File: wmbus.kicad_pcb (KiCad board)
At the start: 2 copper layers, 27 parts, among them IC1 IM871A, J1 480-37-1000, J2 Conn_Coaxial, J3 Conn_01x04_Male, U1 USBLC6-2SC6, U2 XC6206P332MR, U3 CH340E

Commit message: Routing done
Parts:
- added G***: LOGO, LOGO, B.Cu at (105.1, 102.8)
- added kibuzzard-63642CB1: G***, kibuzzard-63642CB1, B.Cu at (108.1, 102.8)
- J2: footprint Connector_Coaxial:SMA_Amphenol_132289_EdgeMount -> wmbus:SMA-SMD_BWSMA-KE-P001
- moved J2 0.74 mm to (119.8, 102.8)
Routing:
- net +3.3V: track 0.00 -> 42.9 mm
- net GND: track 0.00 -> 27.3 mm, vias 0 -> 26
- net /UART_TX: track 0.00 -> 21.4 mm, vias 0 -> 2
- net Net-(D3-Pad2): track 0.00 -> 20.2 mm
- net /UART_RX: track 0.00 -> 18.1 mm, vias 0 -> 2
- net /DBG_CLK: track 0.00 -> 15.7 mm
- net /DBG_DATA: track 0.00 -> 12.9 mm
- net Net-(D2-Pad2): track 0.00 -> 11.9 mm
- net VBUS: track 0.00 -> 9.36 mm
- net Net-(JP2-Pad1): track 0.00 -> 8.10 mm
- net Net-(D1-Pad2): track 0.00 -> 7.48 mm
- net Net-(JP1-Pad1): track 0.00 -> 7.25 mm
- net Net-(C3-Pad1): track 0.00 -> 5.14 mm
- net /USB_CONN_D-: track 0.00 -> 3.61 mm
- net /USB_CONN_D+: track 0.00 -> 3.61 mm
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
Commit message: Ready for production rev1
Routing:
- net Net-(IC1-Pad16): track 0.00 -> 13.3 mm
- net GND: track 27.3 -> 30.3 mm, vias 26 -> 59
- added copper zone on In1.Cu, net GND
- added copper zone on In2.Cu, net GND
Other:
- board outline added: 56.6 x 20 mm
- copper layers 2 -> 4

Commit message: Added antenna 3D model, removed useless GND via, unified via size
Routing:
- net GND: track 30.3 -> 28.7 mm, vias 59 -> 58
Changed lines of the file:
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@@
     (pad "5" smd rect (at 0 2.55) (size 5 1.2) (layers "F.Cu" "F.Paste" "F.Mask")
       (net 16 "GND") (pinfunction "Ext") (pintype "passive"))
+    (model "${KIPRJMOD}/3D/antenna.wrl"
+      (offset (xyz 0 0 -4))
+      (scale (xyz 0.4 0.4 0.4))
+      (rotate (xyz 0 0 90))
+    )
   )
   (footprint "wmbus:MOLEX_480-37-1000" (layer "F.Cu")
@@
     (property "Sheetname" "")
     (attr through_hole)
-    (fp_text reference "J1" (at -2.825 -6.635 -90) (layer "F.SilkS")
+    (fp_text reference "J1" (at -2.825 -6.635 -90) (layer "F.SilkS") hide
       (effects (font (size 1 1) (thickness 0.15)))
     )
@@
   (segment (start 110.35 93.825) (end 110.35 94.925) (width 0.3) (layer "F.Cu") (net 16))
   (segment (start 84 109.575) (end 84 110.525) (width 0.3) (layer "F.Cu") (net 16))
-  (segment (start 82.575 95.65) (end 82.185 95.65) (width 0.3) (layer "F.Cu") (net 16))
   (segment (start 88.075 105.8) (end 87.1 105.8) (width 0.3) (layer "F.Cu") (net 16))
   (segment (start 77.025 109.575) (end 77.025 110.55) (width 0.3) (layer "F.Cu") (net 16))
@@
   (segment (start 86.185 110.175) (end 85.25 110.175) (width 0.3) (layer "F.Cu") (net 16))
   (segment (start 97.75 97.225) (end 96.475 97.225) (width 0.3) (layer "F.Cu") (net 16))
-  (segment (start 83.45 96.525) (end 82.575 95.65) (width 0.3) (layer "F.Cu") (net 16))
   (segment (start 86.185 108.575) (end 85.25 108.575) (width 0.3) (layer "F.Cu") (net 16))
   (segment (start 74.5625 102.5) (end 73.25 102.5) (width 0.3) (layer "F.Cu") (net 16))
   (segment (start 96.475 97.225) (end 96.45 97.2) (width 0.3) (layer "F.Cu") (net 16))
   (segment (start 85.25 110.175) (end 85.225 110.15) (width 0.3) (layer "F.Cu") (net 16))
-  (segment (start 75.5 109.575) (end 75.5 110.55) (width 0.3) (layer "F.Cu") (net 16))
   (segment (start 85.3 111.775) (end 86.185 111.775) (width 0.3) (layer "F.Cu") (net 16))
   (segment (start 119.75 99.125) (end 119.75 100.275) (width 0.3) (layer "F.Cu") (net 16))
@@
   (segment (start 95.27 104.72) (end 95.27 105.675) (width 0.3) (layer "F.Cu") (net 16))
   (segment (start 97.75 105.625) (end 96.525 105.625) (width 0.3) (layer "F.Cu") (net 16))
-  (segment (start 80.6875 110.7625) (end 80.675 110.775) (width 0.3) (layer "F.Cu") (net 16))
   (segment (start 114.55 94.925) (end 114.55 93.85) (width 0.3) (layer "F.Cu") (net 16))
   (segment (start 71.1 99) (end 71.1 97.875) (width 0.3) (layer "F.Cu") (net 16))
@@
   (segment (start 79.425 103.25) (end 80.675 103.25) (width 0.3) (layer "F.Cu") (net 16))
   (segment (start 85.275 111.75) (end 85.3 111.775) (width 0.3) (layer "F.Cu") (net 16))
+  (segment (start 75.5 109.575) (end 75.5 110.55) (width 0.3) (layer "F.Cu") (net 16))
   (segment (start 93.72 104.72) (end 93.72 105.675) (width 0.3) (layer "F.Cu") (net 16))
   (via (at 115.525 108.4) (size 0.7) (drill 0.3) (layers "F.Cu" "B.Cu") (net 16))
@@
   (via (at 119.725 96.125) (size 0.7) (drill 0.3) (layers "F.Cu" "B.Cu") (net 16))
   (via (at 96.45 97.2) (size 0.7) (drill 0.3) (layers "F.Cu" "B.Cu") (net 16))
-  (via (at 75.5 110.55) (size 0.8) (drill 0.4) (layers "F.Cu" "B.Cu") (net 16))
   (via (at 72.7 99) (size 0.7) (drill 0.3) (layers "F.Cu" "B.Cu") (net 16))
   (via (at 113.825 111.675) (size 0.7) (drill 0.3) (layers "F.Cu" "B.Cu") (net 16))
-  (via (at 80.675 110.775) (size 0.8) (drill 0.4) (layers "F.Cu" "B.Cu") (net 16))
-  (via (at 83.45 96.525) (size 0.7) (drill 0.3) (layers "F.Cu" "B.Cu") (net 16))
   (via (at 87.35 99.725) (size 0.7) (drill 0.3) (layers "F.Cu" "B.Cu") (net 16))
   (via (at 75.425 97.4) (size 0.7) (drill 0.3) (layers "F.Cu" "B.Cu") (net 16))
@@
   (via (at 115.725 103.575) (size 0.7) (drill 0.3) (layers "F.Cu" "B.Cu") (net 16))
   (via (at 78.8 111.475) (size 0.7) (drill 0.3) (layers "F.Cu" "B.Cu") (net 16))
+  (via (at 80.6875 110.7625) (size 0.7) (drill 0.3) (layers "F.Cu" "B.Cu") (net 16))
   (via (at 119.65 109.875) (size 0.7) (drill 0.3) (layers "F.Cu" "B.Cu") (net 16))
   (via (at 88.1 104.275) (size 0.7) (drill 0.3) (layers "F.Cu" "B.Cu") (net 16))
@@
   (via (at 95.25 104.7) (size 0.7) (drill 0.3) (layers "F.Cu" "B.Cu") (net 16))
   (via (at 85.275 111.75) (size 0.7) (drill 0.3) (layers "F.Cu" "B.Cu") (net 16))
-  (via (at 77.025 110.55) (size 0.8) (drill 0.4) (layers "F.Cu" "B.Cu") (net 16))
   (via (at 94.275 95.05) (size 0.7) (drill 0.3) (layers "F.Cu" "B.Cu") (net 16))
   (via (at 110.925 111.625) (size 0.7) (drill 0.3) (layers "F.Cu" "B.Cu") (net 16))
   (via (at 93.7 104.7) (size 0.7) (drill 0.3) (layers "F.Cu" "B.Cu") (net 16))
+  (via (at 75.5 110.55) (size 0.7) (drill 0.3) (layers "F.Cu" "B.Cu") (net 16))
   (via (at 119.75 99.125) (size 0.7) (drill 0.3) (layers "F.Cu" "B.Cu") (net 16))
   (via (at 78.875 106.1) (size 0.7) (drill 0.3) (layers "F.Cu" "B.Cu") (free) (net 16))
@@
   (via (at 85.225 110.15) (size 0.7) (drill 0.3) (layers "F.Cu" "B.Cu") (net 16))
   (via (at 117.525 97.425) (size 0.7) (drill 0.3) (layers "F.Cu" "B.Cu") (net 16))
+  (via (at 77.025 110.55) (size 0.7) (drill 0.3) (layers "F.Cu" "B.Cu") (net 16))
   (via (at 85.25 108.575) (size 0.7) (drill 0.3) (layers "F.Cu" "B.Cu") (net 16))
   (via (at 88.075 101.8) (size 0.7) (drill 0.3) (layers "F.Cu" "B.Cu") (net 16))

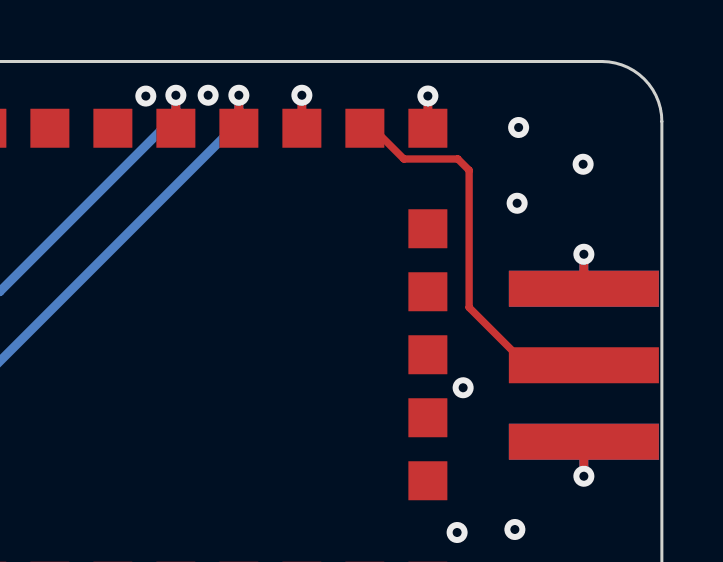
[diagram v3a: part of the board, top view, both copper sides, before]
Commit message: Rounded RF track
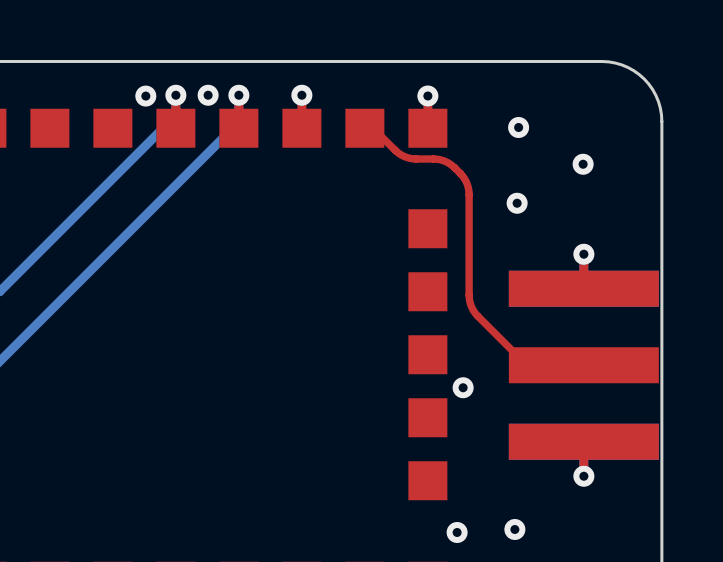
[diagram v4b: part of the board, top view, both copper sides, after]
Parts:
- removed kibuzzard-63642CB1: G***, kibuzzard-63642CB1
- added kibuzzard-636EC376: G***, kibuzzard-636EC376, B.Cu at (108.1, 102.8)

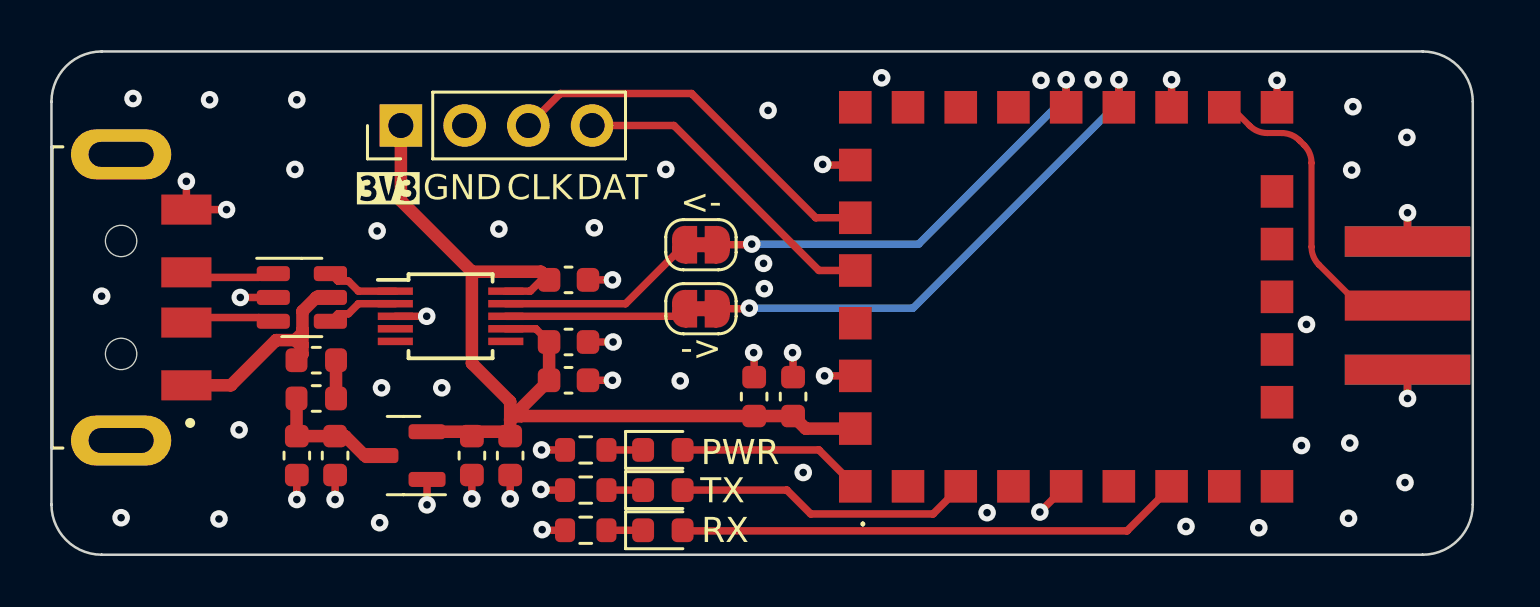
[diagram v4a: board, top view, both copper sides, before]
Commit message: rev2 - smaller, removed unused rx/tx jumpers
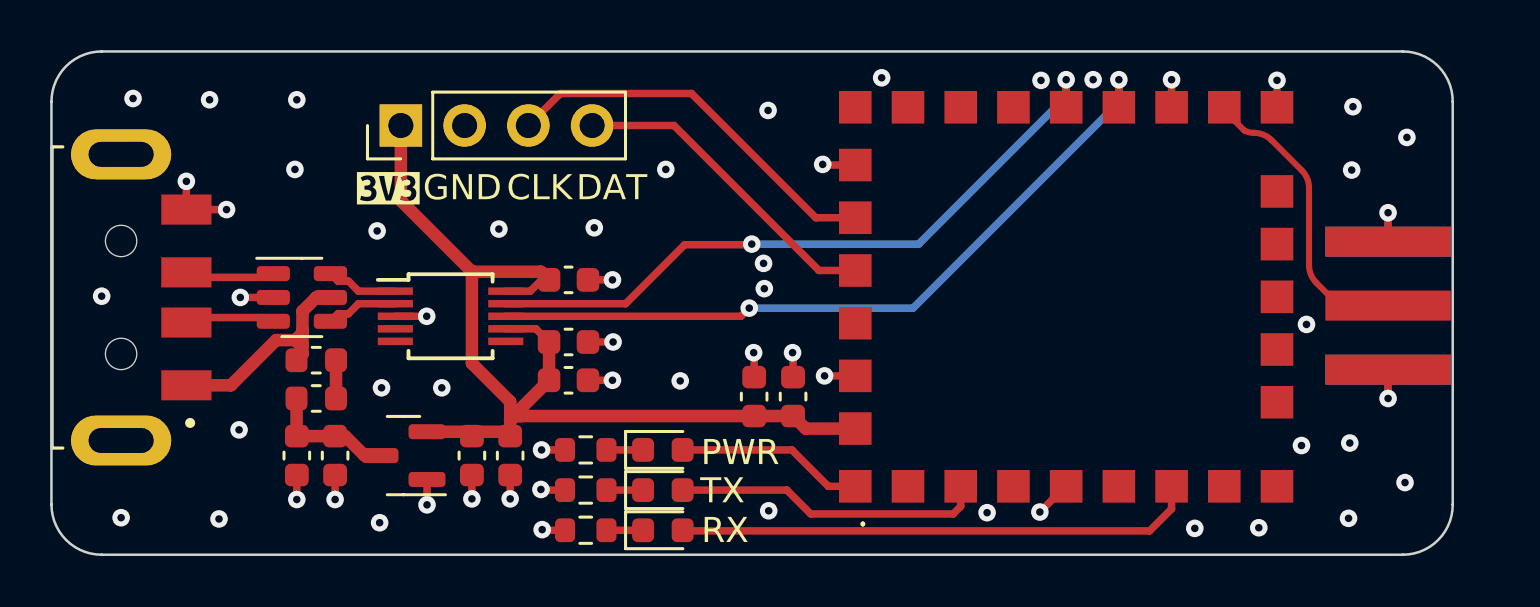
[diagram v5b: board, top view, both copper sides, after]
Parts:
- removed JP1, JP2: SolderJumper_2_Bridged, Jumper:SolderJumper-2_P1.3mm_Bridged_RoundedPad1.0x1.5mm
- moved J2 0.78 mm to (119.0, 102.8)
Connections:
- U3 pad 8: Net-(JP1-Pad1) -> /UART_TX
- U3 pad 9: Net-(JP2-Pad1) -> /UART_RX
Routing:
- net /UART_RX: track 18.1 -> 27.5 mm
- net /UART_TX: track 21.4 -> 30.0 mm
- net Net-(JP2-Pad1): track 8.10 -> 0.00 mm
- net Net-(JP1-Pad1): track 7.25 -> 0.00 mm
- net Net-(IC1-Pad16): track 12.8 -> 12.0 mm
- net Net-(D3-Pad2): track 20.2 -> 20.8 mm
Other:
- board size 56.6 x 20 mm -> 55.8 x 20 mm
- board text removed: "->"
- board text removed: "<-"
